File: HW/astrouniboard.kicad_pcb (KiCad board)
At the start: 2 copper layers, 35 x 42 mm, 140 parts, among them J10 Conn_01x04, J2 MC-311D, J3 Conn_01x04, J4 Conn_01x03, J5 Conn_01x04, J6 5.5/2.1 Barell DC2, J7 MC-311D, J8 Conn_01x04, J9 Conn_01x04, U1 ME6231, U10 MPU-6000, U11 CH213K, U12 ME3116, U13 CH213K, U14 CH213K, U4 24AA64T-I/OT, U5 STM32G0B1CBTx, U6 CH334P, U7 USBLC6-2SC6, U8 SHT31A-DIS, Y1 TAXM8M4RDBCCT2T / 8MHz, Y2 TAXM12M4RDBCCT2T / 12MHz

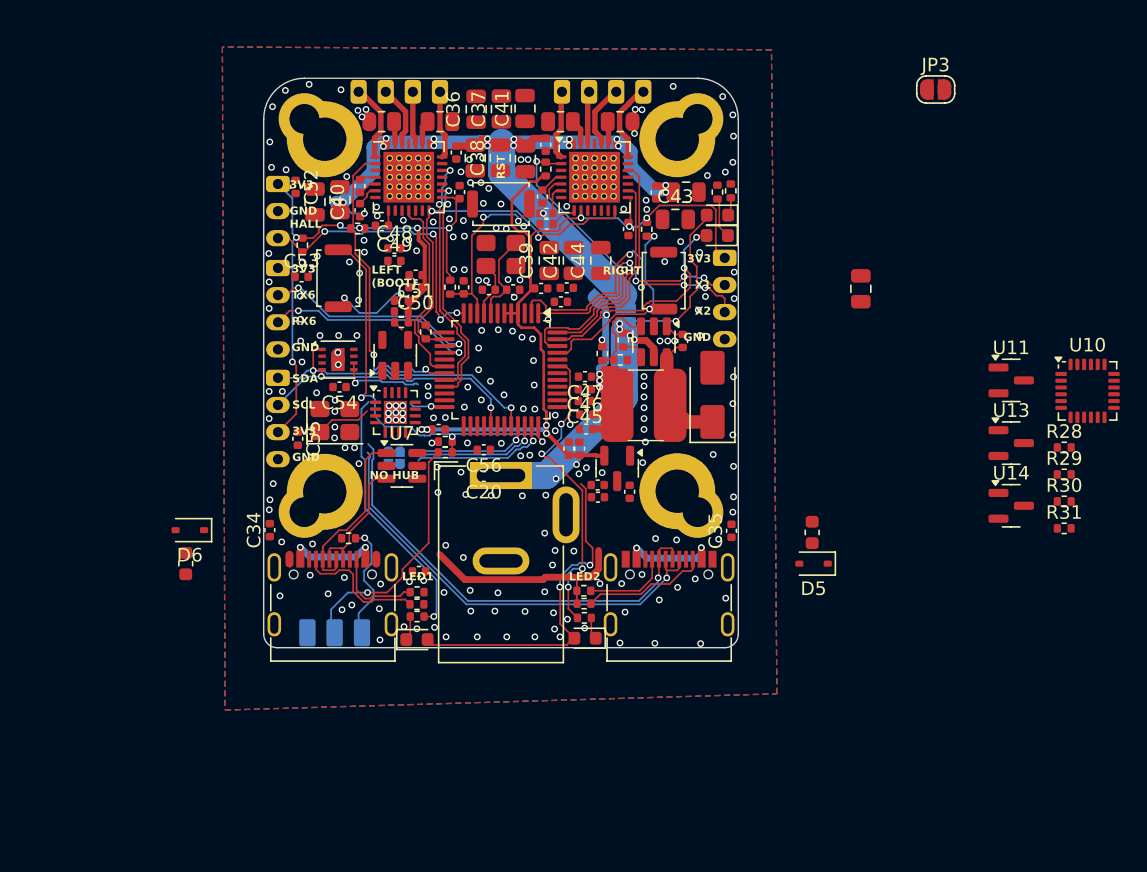
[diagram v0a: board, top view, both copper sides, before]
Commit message: hw: upgrade KiCad project to v10 format
Update PCB, schematic, and project files to KiCad 10 format (generator_version 10.0).
Add .kicad_prl local layout rules file. Exclude .history/ backup dir from git.

Co-Authored-By: Claude Sonnet 4.6 <noreply@anthropic.com>
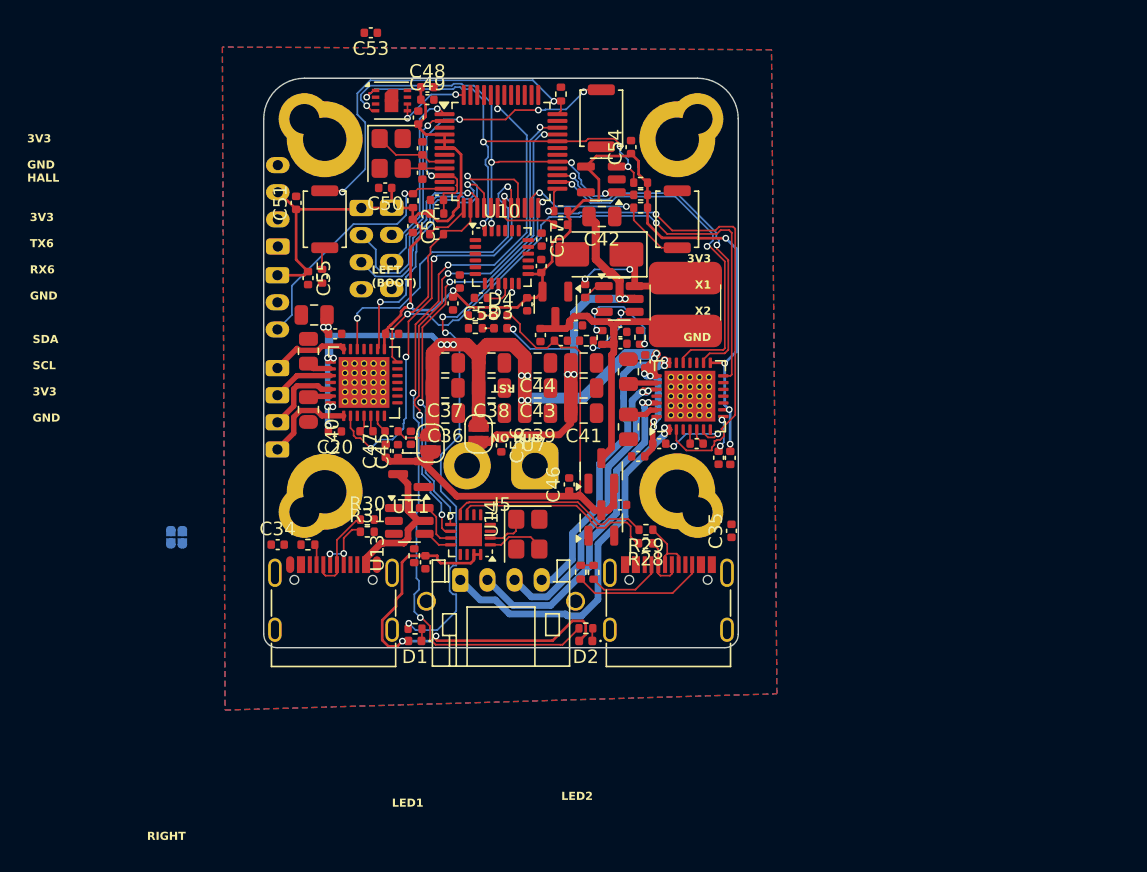
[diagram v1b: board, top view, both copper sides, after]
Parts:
- removed D5, D6: 1N5819WS, Diode_SMD:D_SOD-323
- removed F1, F2: SMD0603P050TF, Fuse:Fuse_0603_1608Metric
- removed JP3: SolderJumper_2_Open, Jumper:SolderJumper-2_P1.3mm_Open_RoundedPad1.0x1.5mm
- removed R1, R2: 22R, Resistor_SMD:R_0402_1005Metric
- removed TP1, TP2, TP3: TestPoint, myLib_SMD:TestPoint_Micro
- added C57: 2n2, Capacitor_SMD:C_0402_1005Metric, F.Cu at (85.5, 101.9)
- added C58: 100n, Capacitor_SMD:C_0402_1005Metric, F.Cu at (81.1, 106.2)
- D1, D2, D3, D4: footprint LED_SMD:LED_0603_1608Metric -> LED_SMD:LED_0402_1005Metric
- J5: footprint Connector_JST:JST_PH_B4B-PH-K_1x04_P2.00mm_Vertical -> Connector_JST:JST_PH_S4B-PH-K_1x04_P2.00mm_Horizontal
- J6: footprint Connector_BarrelJack:BarrelJack_GCT_DCJ200-10-A_Horizontal -> Connector_AMASS:AMASS_XT30PW-M_1x02_P2.50mm_Horizontal; moved to B.Cu
- JP4, JP5: moved to F.Cu
- moved R30 51.4 mm to (72.7, 122.5)
- moved R31 51.4 mm to (72.7, 123.5)
- moved U11 44.8 mm to (75.9, 119.2), turned to 180 degrees
- moved U10 44.3 mm to (82.6, 103.2)
- moved J5 36.8 mm to (79.5, 127.0)
- moved R28 31.7 mm to (93.2, 124.3), turned to 180 degrees
- moved R29 31.1 mm to (93.2, 123.3), turned to 180 degrees
- moved U13 30.8 mm to (90.0, 122.8), turned to 90 degrees
- moved U14 30.3 mm to (90.0, 119.0), turned to 90 degrees
- moved C3 28.9 mm to (68.8, 107.5), turned to 0 degrees
- moved C54 27.8 mm to (92.1, 95.1), turned to 90 degrees
- moved J3 27.1 mm to (66.1, 117.4), turned to 90 degrees
- moved R4 27.0 mm to (87.0, 91.2), turned to -90 degrees
- moved J8 24.8 mm to (74.5, 99.5)
- moved C40 23.1 mm to (88.7, 111.0), turned to 180 degrees
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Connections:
- C11 pad 1: +5V -> +5V3
- C12 pad 1: +5V -> +5V3
- C31 pad 1: +5V -> +5V3
- C32 pad 1: +5V -> +5V3
- C36 pad 1: unconnected-(C36-Pad1) -> GND
- C36 pad 2: unconnected-(C36-Pad2) -> Vdrive1
- C37 pad 1: unconnected-(C37-Pad1) -> GND
- C37 pad 2: unconnected-(C37-Pad2) -> Vdrive1
- C38 pad 1: unconnected-(C38-Pad1) -> GND
- C38 pad 2: unconnected-(C38-Pad2) -> Vdrive1
- C39 pad 1: unconnected-(C39-Pad1) -> GND
- C39 pad 2: unconnected-(C39-Pad2) -> Vdrive1
- C40 pad 1: unconnected-(C40-Pad1) -> GND
- C40 pad 2: unconnected-(C40-Pad2) -> +12V
- C41 pad 1: unconnected-(C41-Pad1) -> GND
- C41 pad 2: unconnected-(C41-Pad2) -> +12V
- C42 pad 1: unconnected-(C42-Pad1) -> GND
- C42 pad 2: unconnected-(C42-Pad2) -> +12V
- C43 pad 1: unconnected-(C43-Pad1) -> GND
- C43 pad 2: unconnected-(C43-Pad2) -> Vdrive1
- C44 pad 1: unconnected-(C44-Pad1) -> GND
- C44 pad 2: unconnected-(C44-Pad2) -> Vdrive1
- J2 pad A4: Net-(D6-A) -> VUSB_UPSTREAM
- J2 pad A9: Net-(D6-A) -> VUSB_UPSTREAM
- J2 pad B4: Net-(D6-A) -> VUSB_UPSTREAM
- J2 pad B9: Net-(D6-A) -> VUSB_UPSTREAM
- J6 pad 1: +12V -> GND
- J6 pad 2: GND -> +12V
- J7 pad A4: Net-(D5-K) -> Net-(U13-OUT)
- J7 pad A9: Net-(D5-K) -> Net-(U13-OUT)
- J7 pad B4: Net-(D5-K) -> Net-(U13-OUT)
- J7 pad B9: Net-(D5-K) -> Net-(U13-OUT)
- L4 pad 2: +5V -> +5V3
- R15 pad 1: Net-(U5-PB6) -> Net-(U5-PB11)
- R22 pad 2: +5V -> +5V3
- RIGHT1 pad 2: Net-(U5-PB6) -> Net-(U5-PB11)
- U1 pad 3: +5V -> +5V3
- U10 pad 1: unconnected-(U10-CLKIN-Pad1) -> GND
- U10 pad 10: unconnected-(U10-REGOUT-Pad10) -> Net-(U10-REGOUT)
- U10 pad 11: unconnected-(U10-FSYNC-Pad11) -> GND
- U10 pad 13: unconnected-(U10-VDD-Pad13) -> +3.3V
- U10 pad 18: unconnected-(U10-GND-Pad18) -> GND
- U10 pad 20: unconnected-(U10-CPOUT-Pad20) -> Net-(U10-CPOUT)
- U10 pad 23: unconnected-(U10-SCL/SCLK-Pad23) -> SCL
- U10 pad 24: unconnected-(U10-SDA/MOSI-Pad24) -> SDA
- U10 pad 9: unconnected-(U10-AD0/MISO-Pad9) -> GND
- U11 pad 1: (no net) -> GND
- U11 pad 2: unconnected-(U11-OUT-Pad2) -> +5V
- U11 pad 3: unconnected-(U11-GND-Pad3) -> VUSB_UPSTREAM
- U13 pad 1: (no net) -> GND
- U13 pad 2: unconnected-(U13-OUT-Pad2) -> Net-(U13-OUT)
- U13 pad 3: unconnected-(U13-GND-Pad3) -> +5V
- U14 pad 1: (no net) -> GND
- U14 pad 2: unconnected-(U14-OUT-Pad2) -> +5V
- U14 pad 3: unconnected-(U14-GND-Pad3) -> +5V3
- U5 pad 18: DIAG -> unconnected-(U5-PA7-Pad18)
- U5 pad 23: unconnected-(U5-PB11-Pad23) -> Net-(U5-PB11)
- U5 pad 25: unconnected-(U5-PB13-Pad25) -> EN2
- U5 pad 26: unconnected-(U5-PB14-Pad26) -> DIR2
- U5 pad 27: unconnected-(U5-PB15-Pad27) -> STEP2
- U5 pad 45: Net-(U5-PB6) -> unconnected-(U5-PB6-Pad45)
- U5 pad 46: EN2 -> unconnected-(U5-PB7-Pad46)
- U5 pad 47: DIR2 -> unconnected-(U5-PB8-Pad47)
- U5 pad 48: STEP2 -> Net-(U5-PB9)
- U7 pad 5: Net-(D6-A) -> VUSB_UPSTREAM
- U8 pad 5: +3.3V -> Net-(U5-PB9)
- U8 pad 6: +3.3V -> Net-(U5-PB9)
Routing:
- net Net-(U5-PB4): track 22.2 -> 59.3 mm
- net Net-(J7-D--PadA7): track 33.5 -> 4.20 mm, vias 1 -> 0
- net /DP: track 9.60 -> 38.1 mm, vias 1 -> 4
- net Net-(J7-D+-PadA6): track 32.9 -> 4.64 mm, vias 1 -> 0
- net /DM: track 8.91 -> 36.2 mm, vias 1 -> 4
- net TMC_UART: track 27.8 -> 54.6 mm
- net +5V3: track 0.00 -> 23.3 mm
- net Net-(J5-Pin_1): track 5.06 -> 28.2 mm, vias 0 -> 2
- net Net-(J5-Pin_2): track 3.74 -> 24.4 mm, vias 0 -> 2
- net Net-(U5-PB12): track 21.8 -> 41.6 mm, vias 2 -> 4
- net Net-(J5-Pin_3): track 4.64 -> 23.9 mm, vias 0 -> 2
- net /SWDCLK: track 18.0 -> 0.00 mm, vias 1 -> 0
- net Net-(J5-Pin_4): track 5.70 -> 23.3 mm, vias 0 -> 2
- net Net-(U5-PB6): track 17.0 -> 0.00 mm, vias 2 -> 0
- net Vdrive1: track 62.8 -> 78.3 mm, vias 18 -> 20
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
